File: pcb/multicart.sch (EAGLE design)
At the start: 13 parts, among them IC1 74HCT373N, IC2 M27C4001B, Q1 BS170

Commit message: Changed cart connector package & removed unused signals.
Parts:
- J1: device atari-800:ATARI-800-MEDIUM -> atari-800:ATARI-800
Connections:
- net D6: no longer IC1A.2D
- net D7: no longer IC1A.1D
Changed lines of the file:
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@@
 </classes>
 <parts>
-<part name="J1" library="atari-800" deviceset="ATARI-800" device="-MEDIUM"/>
+<part name="J1" library="atari-800" deviceset="ATARI-800" device=""/>
 <part name="IC1" library="74xx-eu" deviceset="74*373" device="N" technology="HCT"/>
 <part name="IC2" library="st-microelectronics" deviceset="M27C4001" device="B"/>
@@
 <wire x1="132.08" y1="66.04" x2="124.46" y2="66.04" width="0.1524" layer="91"/>
 </segment>
-<segment>
-<pinref part="IC1" gate="A" pin="2D"/>
-<wire x1="22.86" y1="33.02" x2="27.94" y2="33.02" width="0.1524" layer="91"/>
-</segment>
 </net>
 <net name="D7" class="0">
@@
 </segment>
 <segment>
-<pinref part="IC1" gate="A" pin="1D"/>
-<wire x1="22.86" y1="30.48" x2="27.94" y2="30.48" width="0.1524" layer="91"/>
-</segment>
-<segment>

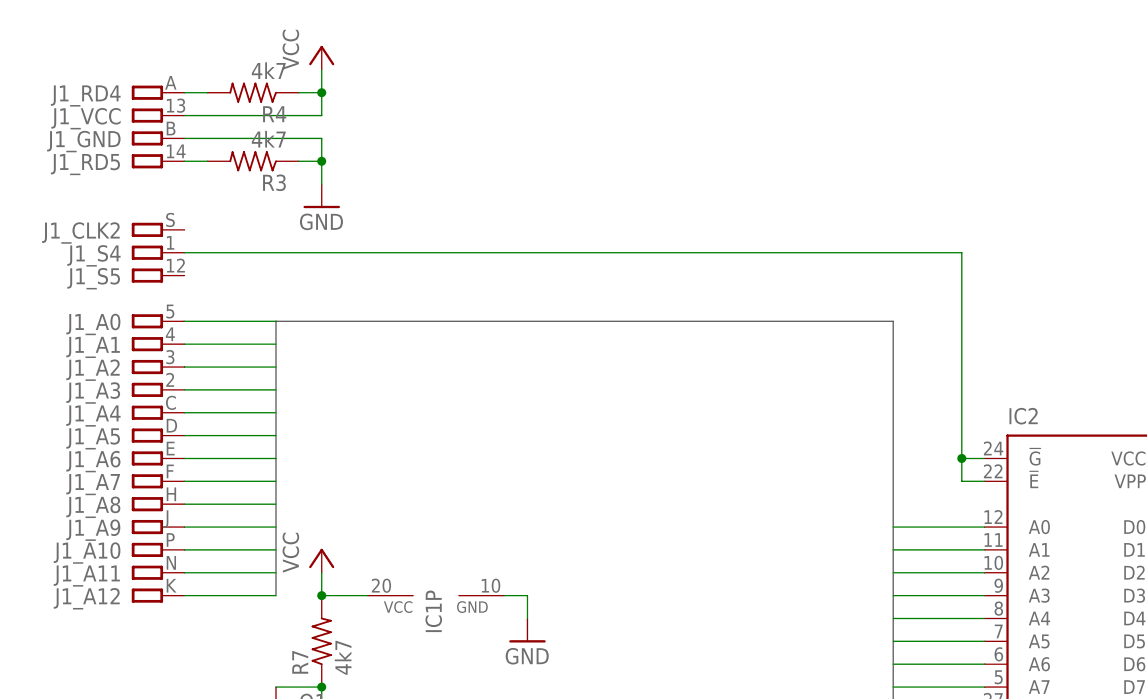
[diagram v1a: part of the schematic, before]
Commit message: Swapped cart bank mapping & reorganized the PCB.
Fixes #1
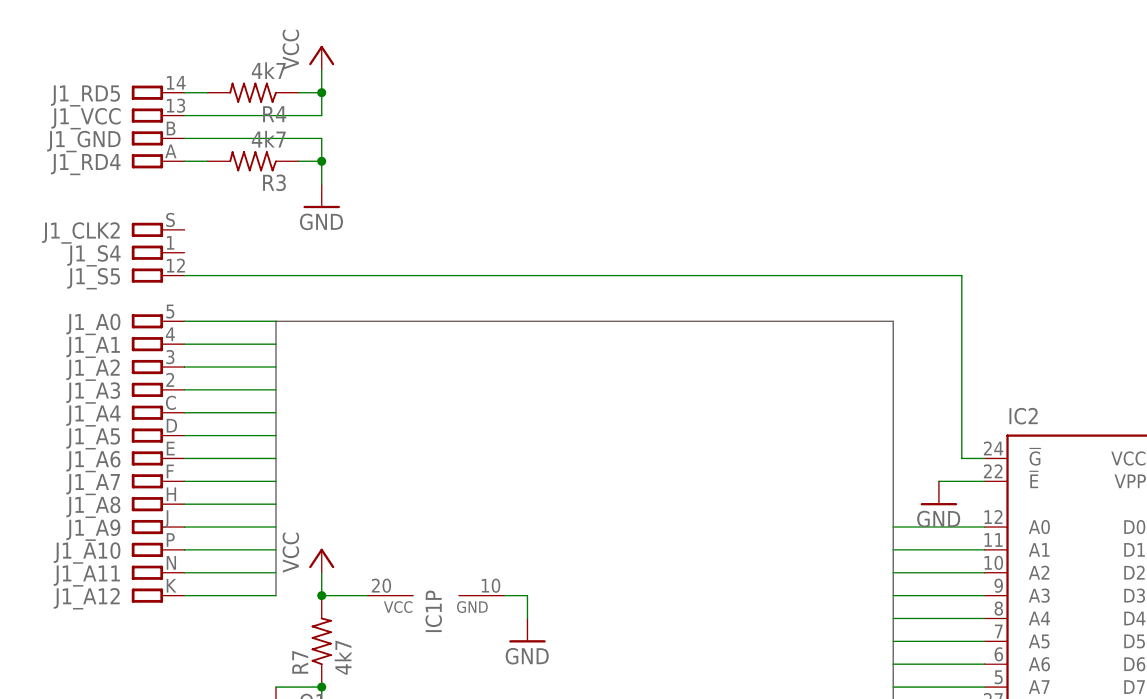
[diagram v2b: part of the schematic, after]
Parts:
- R3: device resistor:R-US_0204/7 -> resistor:R-US_0207/15
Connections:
- net GND: now also IC2.!E
- net N$13: now also J1_RD5.P; no longer J1_RD4.P
- net N$14: now also J1_RD4.P; no longer J1_RD5.P
- net N$17: now also J1_S5.P; no longer IC2.!E, J1_S4.P
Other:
- moved on the sheet: J1_RD4, J1_RD5
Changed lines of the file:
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@@
 <part name="JP2" library="pinhead" deviceset="PINHD-1X3" device=""/>
 <part name="P+5" library="supply1" deviceset="VCC" device=""/>
-<part name="R3" library="resistor" deviceset="R-US_" device="0204/7" value="4k7"/>
+<part name="R3" library="resistor" deviceset="R-US_" device="0207/15" value="4k7"/>
 <part name="R4" library="resistor" deviceset="R-US_" device="0204/7" value="4k7"/>
 <part name="JP1" library="pinhead" deviceset="PINHD-1X3" device=""/>
@@
 <part name="Q1" library="transistor-small-signal" deviceset="BS170" device=""/>
 <part name="R7" library="resistor" deviceset="R-US_" device="0204/7" value="4k7"/>
+<part name="GND3" library="supply1" deviceset="GND" device=""/>
 </parts>
 <sheets>
@@
 <instance part="J1" gate="_A5" x="10.16" y="91.44" rot="MR0"/>
 <instance part="J1" gate="_A4" x="10.16" y="93.98" rot="MR0"/>
-<instance part="J1" gate="_RD4" x="10.16" y="129.54" rot="MR0"/>
-<instance part="J1" gate="_RD5" x="10.16" y="121.92" rot="MR0"/>
+<instance part="J1" gate="_RD4" x="10.16" y="121.92" rot="MR0"/>
+<instance part="J1" gate="_RD5" x="10.16" y="129.54" rot="MR0"/>
 <instance part="J1" gate="_CCTL" x="10.16" y="58.42" rot="MR0"/>
 <instance part="J1" gate="_A10" x="10.16" y="78.74" rot="MR0"/>
@@
 <instance part="Q1" gate="1" x="20.32" y="58.42"/>
 <instance part="R7" gate="G$1" x="27.94" y="68.58" rot="R90"/>
+<instance part="GND3" gate="1" x="96.52" y="83.82"/>
 </instances>
 <busses>
@@
 <junction x="27.94" y="121.92"/>
 </segment>
+<segment>
+<pinref part="IC2" gate="G$1" pin="!E"/>
+<pinref part="GND3" gate="1" pin="GND"/>
+<wire x1="101.6" y1="86.36" x2="96.52" y2="86.36" width="0.1524" layer="91"/>
+</segment>
 </net>
 <net name="N$9" class="0">
@@
 </segment>
 </net>
-<net name="N$13" class="0">
-<segment>
-<pinref part="J1" gate="_RD4" pin="P"/>
-<pinref part="R4" gate="G$1" pin="2"/>
-<wire x1="12.7" y1="129.54" x2="15.24" y2="129.54" width="0.1524" layer="91"/>
-</segment>
-</net>
-<net name="N$14" class="0">
-<segment>
-<pinref part="R3" gate="G$1" pin="2"/>
-<pinref part="J1" gate="_RD5" pin="P"/>
-<wire x1="15.24" y1="121.92" x2="12.7" y2="121.92" width="0.1524" layer="91"/>
-</segment>
-</net>
 <net name="N$6" class="0">
 <segment>
@@
 <net name="N$17" class="0">
 <segment>
-<pinref part="IC2" gate="G$1" pin="!E"/>
-<wire x1="101.6" y1="86.36" x2="99.06" y2="86.36" width="0.1524" layer="91"/>
-<pinref part="J1" gate="_S4" pin="P"/>
-<wire x1="12.7" y1="111.76" x2="99.06" y2="111.76" width="0.1524" layer="91"/>
-<wire x1="99.06" y1="111.76" x2="99.06" y2="88.9" width="0.1524" layer="91"/>
 <pinref part="IC2" gate="G$1" pin="!G"/>
 <wire x1="99.06" y1="88.9" x2="101.6" y2="88.9" width="0.1524" layer="91"/>
-<wire x1="99.06" y1="86.36" x2="99.06" y2="88.9" width="0.1524" layer="91"/>
-<junction x="99.06" y="88.9"/>
+<pinref part="J1" gate="_S5" pin="P"/>
+<wire x1="12.7" y1="109.22" x2="99.06" y2="109.22" width="0.1524" layer="91"/>
+<wire x1="99.06" y1="109.22" x2="99.06" y2="88.9" width="0.1524" layer="91"/>
 </segment>
 </net>
@@
 </segment>
 </net>
+<net name="N$13" class="0">
+<segment>
+<pinref part="J1" gate="_RD5" pin="P"/>
+<pinref part="R4" gate="G$1" pin="2"/>
+<wire x1="12.7" y1="129.54" x2="15.24" y2="129.54" width="0.1524" layer="91"/>
+</segment>
+</net>
+<net name="N$14" class="0">
+<segment>
+<pinref part="J1" gate="_RD4" pin="P"/>
+<pinref part="R3" gate="G$1" pin="2"/>
+<wire x1="12.7" y1="121.92" x2="15.24" y2="121.92" width="0.1524" layer="91"/>
+</segment>
+</net>
 </nets>
 </sheet>
 </sheets>
+<errors>
+</errors>
 </schematic>
 </drawing>

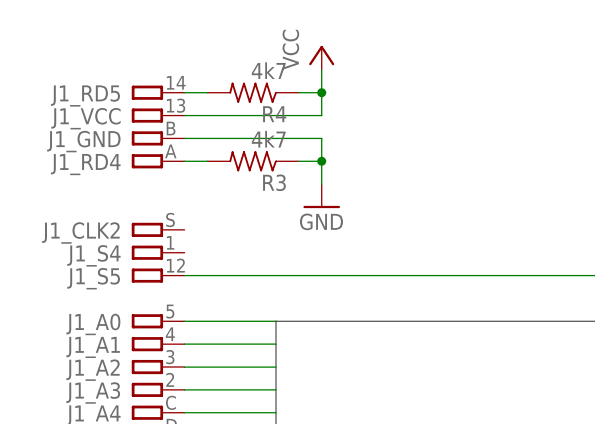
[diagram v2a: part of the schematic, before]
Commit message: Optimized the design.
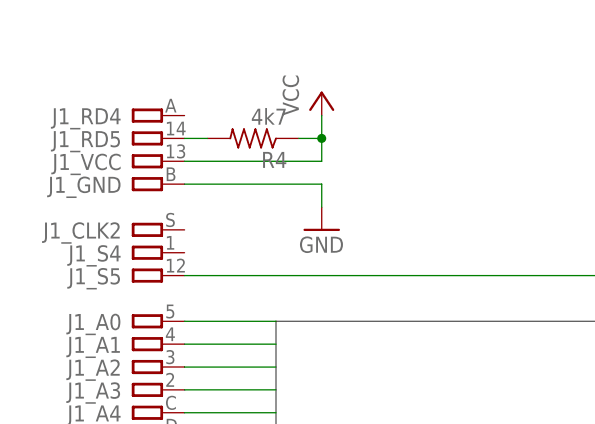
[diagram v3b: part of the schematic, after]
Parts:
- removed R3: 4k7, resistor:R-US_0207/15
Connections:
- removed net N$14: J1_RD4.P, R3.2
- net GND: no longer R3.1
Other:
- moved on the sheet: J1_GND, J1_RD4, J1_RD5, J1_VCC, R4
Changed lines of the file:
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@@
 <part name="JP2" library="pinhead" deviceset="PINHD-1X3" device=""/>
 <part name="P+5" library="supply1" deviceset="VCC" device=""/>
-<part name="R3" library="resistor" deviceset="R-US_" device="0207/15" value="4k7"/>
 <part name="R4" library="resistor" deviceset="R-US_" device="0204/7" value="4k7"/>
 <part name="JP1" library="pinhead" deviceset="PINHD-1X3" device=""/>
@@
 <instance part="J1" gate="_A5" x="10.16" y="91.44" rot="MR0"/>
 <instance part="J1" gate="_A4" x="10.16" y="93.98" rot="MR0"/>
-<instance part="J1" gate="_RD4" x="10.16" y="121.92" rot="MR0"/>
-<instance part="J1" gate="_RD5" x="10.16" y="129.54" rot="MR0"/>
+<instance part="J1" gate="_RD4" x="10.16" y="127" rot="MR0"/>
+<instance part="J1" gate="_RD5" x="10.16" y="124.46" rot="MR0"/>
 <instance part="J1" gate="_CCTL" x="10.16" y="58.42" rot="MR0"/>
 <instance part="J1" gate="_A10" x="10.16" y="78.74" rot="MR0"/>
 <instance part="J1" gate="_R/W" x="10.16" y="55.88" rot="MR0"/>
 <instance part="J1" gate="_CLK2" x="10.16" y="114.3" rot="MR0"/>
-<instance part="J1" gate="_VCC" x="10.16" y="127" rot="MR0"/>
-<instance part="J1" gate="_GND" x="10.16" y="124.46" rot="MR0"/>
+<instance part="J1" gate="_VCC" x="10.16" y="121.92" rot="MR0"/>
+<instance part="J1" gate="_GND" x="10.16" y="119.38" rot="MR0"/>
 <instance part="IC1" gate="A" x="40.64" y="43.18" rot="MR180"/>
 <instance part="IC2" gate="G$1" x="111.76" y="63.5"/>
-<instance part="P+1" gate="VCC" x="27.94" y="134.62"/>
+<instance part="P+1" gate="VCC" x="27.94" y="129.54"/>
 <instance part="P+2" gate="VCC" x="129.54" y="101.6"/>
 <instance part="P+4" gate="VCC" x="27.94" y="78.74"/>
@@
 <instance part="IC1" gate="P" x="40.64" y="73.66" rot="MR270"/>
 <instance part="GND4" gate="1" x="22.86" y="50.8"/>
-<instance part="GND7" gate="1" x="27.94" y="116.84"/>
+<instance part="GND7" gate="1" x="27.94" y="114.3"/>
 <instance part="R1" gate="G$1" x="132.08" y="91.44" rot="R90"/>
 <instance part="R2" gate="G$1" x="60.96" y="22.86" rot="R90"/>
 <instance part="JP2" gate="A" x="71.12" y="12.7" rot="R270"/>
 <instance part="P+5" gate="VCC" x="73.66" y="33.02"/>
-<instance part="R3" gate="G$1" x="20.32" y="121.92" rot="R180"/>
-<instance part="R4" gate="G$1" x="20.32" y="129.54" rot="R180"/>
+<instance part="R4" gate="G$1" x="20.32" y="124.46" rot="R180"/>
 <instance part="JP1" gate="A" x="58.42" y="12.7" rot="R270"/>
 <instance part="P+3" gate="VCC" x="60.96" y="33.02"/>
@@
 <pinref part="J1" gate="_VCC" pin="P"/>
 <pinref part="P+1" gate="VCC" pin="VCC"/>
-<wire x1="12.7" y1="127" x2="27.94" y2="127" width="0.1524" layer="91"/>
-<wire x1="27.94" y1="127" x2="27.94" y2="129.54" width="0.1524" layer="91"/>
+<wire x1="12.7" y1="121.92" x2="27.94" y2="121.92" width="0.1524" layer="91"/>
+<wire x1="27.94" y1="121.92" x2="27.94" y2="124.46" width="0.1524" layer="91"/>
 <pinref part="R4" gate="G$1" pin="1"/>
-<wire x1="27.94" y1="129.54" x2="27.94" y2="132.08" width="0.1524" layer="91"/>
-<wire x1="25.4" y1="129.54" x2="27.94" y2="129.54" width="0.1524" layer="91"/>
-<junction x="27.94" y="129.54"/>
+<wire x1="27.94" y1="124.46" x2="27.94" y2="127" width="0.1524" layer="91"/>
+<wire x1="25.4" y1="124.46" x2="27.94" y2="124.46" width="0.1524" layer="91"/>
+<junction x="27.94" y="124.46"/>
 </segment>
 <segment>
@@
 <pinref part="J1" gate="_GND" pin="P"/>
 <pinref part="GND7" gate="1" pin="GND"/>
-<wire x1="12.7" y1="124.46" x2="27.94" y2="124.46" width="0.1524" layer="91"/>
-<wire x1="27.94" y1="124.46" x2="27.94" y2="121.92" width="0.1524" layer="91"/>
-<pinref part="R3" gate="G$1" pin="1"/>
-<wire x1="27.94" y1="121.92" x2="27.94" y2="119.38" width="0.1524" layer="91"/>
-<wire x1="25.4" y1="121.92" x2="27.94" y2="121.92" width="0.1524" layer="91"/>
-<junction x="27.94" y="121.92"/>
+<wire x1="12.7" y1="119.38" x2="27.94" y2="119.38" width="0.1524" layer="91"/>
+<wire x1="27.94" y1="119.38" x2="27.94" y2="116.84" width="0.1524" layer="91"/>
 </segment>
 <segment>
@@
 <pinref part="J1" gate="_RD5" pin="P"/>
 <pinref part="R4" gate="G$1" pin="2"/>
-<wire x1="12.7" y1="129.54" x2="15.24" y2="129.54" width="0.1524" layer="91"/>
-</segment>
-</net>
-<net name="N$14" class="0">
-<segment>
-<pinref part="J1" gate="_RD4" pin="P"/>
-<pinref part="R3" gate="G$1" pin="2"/>
-<wire x1="12.7" y1="121.92" x2="15.24" y2="121.92" width="0.1524" layer="91"/>
-</segment>
-</net>
+<wire x1="12.7" y1="124.46" x2="15.24" y2="124.46" width="0.1524" layer="91"/>
+</segment>
+</net>

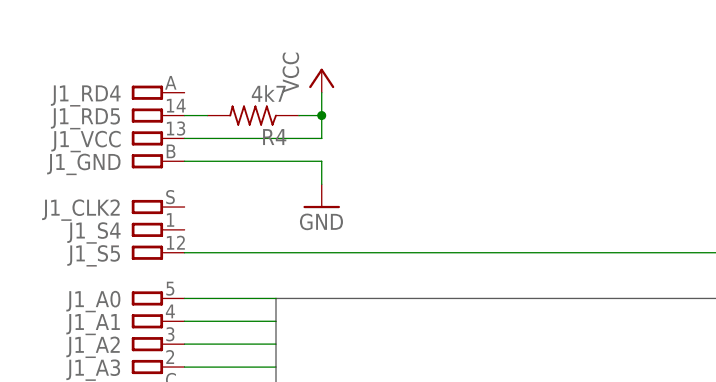
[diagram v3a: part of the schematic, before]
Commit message: Added bypass caps to the design.
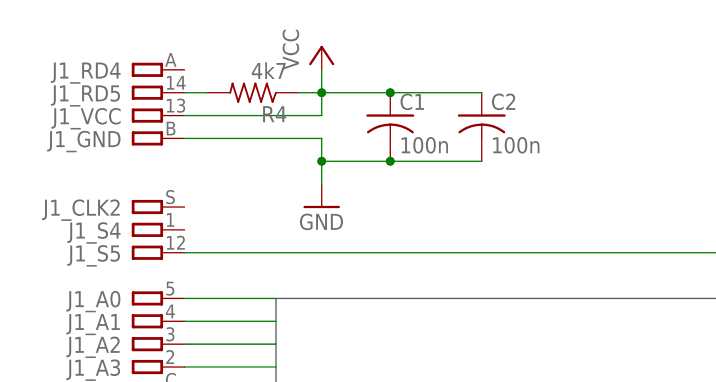
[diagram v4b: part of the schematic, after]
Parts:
- added C1, C2: 100n, resistor:C-US025-025X050
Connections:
- net GND: now also C1.2, C2.2
- net VCC: now also C1.1, C2.1
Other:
- moved on the sheet: J1_GND, J1_RD4, J1_RD5, J1_VCC, R4
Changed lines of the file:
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@@
 <part name="R7" library="resistor" deviceset="R-US_" device="0204/7" value="4k7"/>
 <part name="GND3" library="supply1" deviceset="GND" device=""/>
+<part name="C1" library="resistor" deviceset="C-US" device="025-025X050" value="100n"/>
+<part name="C2" library="resistor" deviceset="C-US" device="025-025X050" value="100n"/>
 </parts>
 <sheets>
@@
 <instance part="J1" gate="_A5" x="10.16" y="91.44" rot="MR0"/>
 <instance part="J1" gate="_A4" x="10.16" y="93.98" rot="MR0"/>
-<instance part="J1" gate="_RD4" x="10.16" y="127" rot="MR0"/>
-<instance part="J1" gate="_RD5" x="10.16" y="124.46" rot="MR0"/>
+<instance part="J1" gate="_RD4" x="10.16" y="129.54" rot="MR0"/>
+<instance part="J1" gate="_RD5" x="10.16" y="127" rot="MR0"/>
 <instance part="J1" gate="_CCTL" x="10.16" y="58.42" rot="MR0"/>
 <instance part="J1" gate="_A10" x="10.16" y="78.74" rot="MR0"/>
 <instance part="J1" gate="_R/W" x="10.16" y="55.88" rot="MR0"/>
 <instance part="J1" gate="_CLK2" x="10.16" y="114.3" rot="MR0"/>
-<instance part="J1" gate="_VCC" x="10.16" y="121.92" rot="MR0"/>
-<instance part="J1" gate="_GND" x="10.16" y="119.38" rot="MR0"/>
+<instance part="J1" gate="_VCC" x="10.16" y="124.46" rot="MR0"/>
+<instance part="J1" gate="_GND" x="10.16" y="121.92" rot="MR0"/>
 <instance part="IC1" gate="A" x="40.64" y="43.18" rot="MR180"/>
 <instance part="IC2" gate="G$1" x="111.76" y="63.5"/>
-<instance part="P+1" gate="VCC" x="27.94" y="129.54"/>
+<instance part="P+1" gate="VCC" x="27.94" y="132.08"/>
 <instance part="P+2" gate="VCC" x="129.54" y="101.6"/>
 <instance part="P+4" gate="VCC" x="27.94" y="78.74"/>
@@
 <instance part="JP2" gate="A" x="71.12" y="12.7" rot="R270"/>
 <instance part="P+5" gate="VCC" x="73.66" y="33.02"/>
-<instance part="R4" gate="G$1" x="20.32" y="124.46" rot="R180"/>
+<instance part="R4" gate="G$1" x="20.32" y="127" rot="R180"/>
 <instance part="JP1" gate="A" x="58.42" y="12.7" rot="R270"/>
 <instance part="P+3" gate="VCC" x="60.96" y="33.02"/>
@@
 <instance part="R7" gate="G$1" x="27.94" y="68.58" rot="R90"/>
 <instance part="GND3" gate="1" x="96.52" y="83.82"/>
+<instance part="C1" gate="G$1" x="35.56" y="124.46"/>
+<instance part="C2" gate="G$1" x="45.72" y="124.46"/>
 </instances>
 <busses>
@@
 <pinref part="J1" gate="_VCC" pin="P"/>
 <pinref part="P+1" gate="VCC" pin="VCC"/>
-<wire x1="12.7" y1="121.92" x2="27.94" y2="121.92" width="0.1524" layer="91"/>
-<wire x1="27.94" y1="121.92" x2="27.94" y2="124.46" width="0.1524" layer="91"/>
+<wire x1="12.7" y1="124.46" x2="27.94" y2="124.46" width="0.1524" layer="91"/>
+<wire x1="27.94" y1="124.46" x2="27.94" y2="127" width="0.1524" layer="91"/>
 <pinref part="R4" gate="G$1" pin="1"/>
-<wire x1="27.94" y1="124.46" x2="27.94" y2="127" width="0.1524" layer="91"/>
-<wire x1="25.4" y1="124.46" x2="27.94" y2="124.46" width="0.1524" layer="91"/>
-<junction x="27.94" y="124.46"/>
+<wire x1="27.94" y1="127" x2="27.94" y2="129.54" width="0.1524" layer="91"/>
+<wire x1="25.4" y1="127" x2="27.94" y2="127" width="0.1524" layer="91"/>
+<junction x="27.94" y="127"/>
+<pinref part="C1" gate="G$1" pin="1"/>
+<wire x1="27.94" y1="127" x2="35.56" y2="127" width="0.1524" layer="91"/>
+<pinref part="C2" gate="G$1" pin="1"/>
+<wire x1="35.56" y1="127" x2="45.72" y2="127" width="0.1524" layer="91"/>
+<junction x="35.56" y="127"/>
 </segment>
 <segment>
@@
 <pinref part="J1" gate="_GND" pin="P"/>
 <pinref part="GND7" gate="1" pin="GND"/>
-<wire x1="12.7" y1="119.38" x2="27.94" y2="119.38" width="0.1524" layer="91"/>
+<wire x1="12.7" y1="121.92" x2="27.94" y2="121.92" width="0.1524" layer="91"/>
+<wire x1="27.94" y1="121.92" x2="27.94" y2="119.38" width="0.1524" layer="91"/>
+<pinref part="C1" gate="G$1" pin="2"/>
 <wire x1="27.94" y1="119.38" x2="27.94" y2="116.84" width="0.1524" layer="91"/>
+<wire x1="27.94" y1="119.38" x2="35.56" y2="119.38" width="0.1524" layer="91"/>
+<pinref part="C2" gate="G$1" pin="2"/>
+<wire x1="35.56" y1="119.38" x2="45.72" y2="119.38" width="0.1524" layer="91"/>
+<junction x="35.56" y="119.38"/>
+<junction x="27.94" y="119.38"/>
 </segment>
 <segment>
@@
 <pinref part="J1" gate="_RD5" pin="P"/>
 <pinref part="R4" gate="G$1" pin="2"/>
-<wire x1="12.7" y1="124.46" x2="15.24" y2="124.46" width="0.1524" layer="91"/>
-</segment>
-</net>
+<wire x1="12.7" y1="127" x2="15.24" y2="127" width="0.1524" layer="91"/>
+</segment>
+</net>
